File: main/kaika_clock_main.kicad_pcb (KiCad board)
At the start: 2 copper layers, 128 x 32 mm, 43 parts, among them J1 Conn_01x04, J6 Conn_01x04, SW1 TC-1102N-C-QL-B, SW2 SW-1101-B-W, SW3 TC-1102N-C-QL-B, U1 AMS1117-3.3, U2 STM32F103C8Tx, U3 DS3231MZ, U4 MICRO-USB_TH, U5 CR1220-2, U6 DS18B20, Y1 Crystal

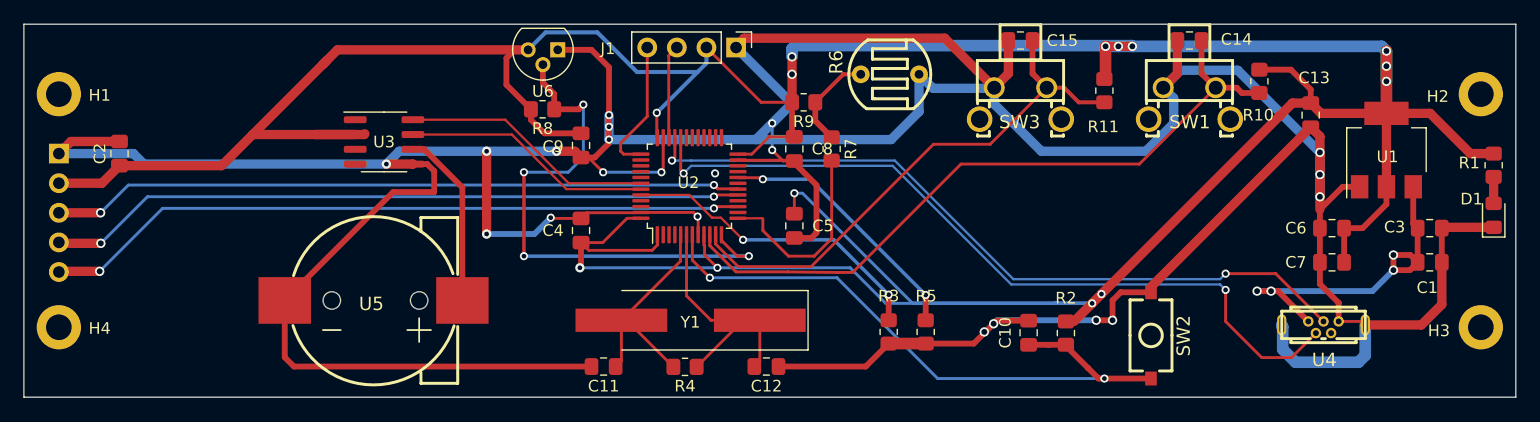
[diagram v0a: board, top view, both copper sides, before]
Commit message: modify the main and display
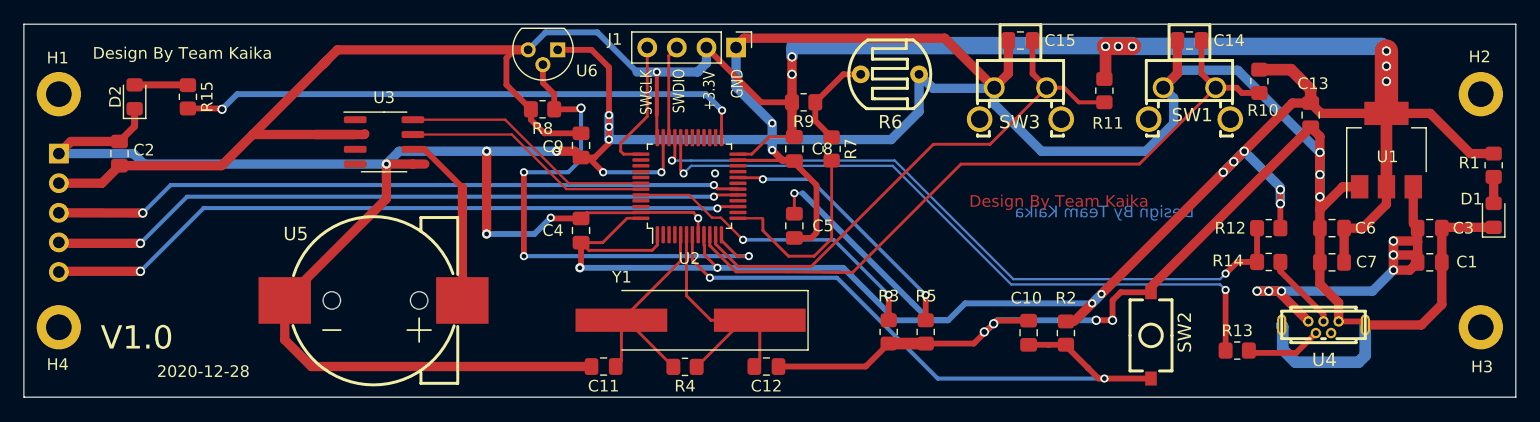
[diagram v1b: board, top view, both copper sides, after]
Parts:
- added D2: LED_Small, LED_SMD:LED_0805_2012Metric_Pad1.15x1.40mm_HandSolder, F.Cu at (109.5, 106.2)
- added R12: 1.5K, Resistor_SMD:R_0805_2012Metric_Pad1.20x1.40mm_HandSolder, F.Cu at (206.8, 117.5)
- added R13: 33, Resistor_SMD:R_0805_2012Metric_Pad1.20x1.40mm_HandSolder, F.Cu at (204.1, 128.0)
- added R14: 33, Resistor_SMD:R_0805_2012Metric_Pad1.20x1.40mm_HandSolder, F.Cu at (206.8, 120.4)
- added R15: 200, Resistor_SMD:R_0805_2012Metric_Pad1.20x1.40mm_HandSolder, F.Cu at (114.1, 106.2)
- J6: value Conn_01x04 -> Conn_01x05
- R6: value RES-GL7528 -> RES-GL7516
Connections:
- U2 pad 25: (no net) -> RUN_LED
- U2 pad 32: USB_D+ -> USB_D-
- U2 pad 33: USB_D- -> USB_D+
- U4 pad 2: USB_D+ -> Net-(R13-Pad1)
- U4 pad 3: USB_D- -> Net-(R14-Pad1)
- U4 pad 7: GND -> (no net)
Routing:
- net RUN_LED: track 0.00 -> 49.4 mm, vias 0 -> 2
- net GND: track 422.9 -> 414.6 mm
- net USB_D+: track 67.0 -> 60.0 mm
- net Net-(R14-Pad1): track 0.00 -> 6.63 mm
- net Net-(R13-Pad1): track 0.00 -> 6.54 mm
- net VCC: track 30.5 -> 36.2 mm, vias 4 -> 6
- net Net-(D2-Pad2): track 0.00 -> 4.58 mm
- net USB_D-: track 64.1 -> 59.5 mm
- net DS18B20: track 46.9 -> 46.2 mm
- net +3V3: track 351.6 -> 351.3 mm, vias 14 -> 19
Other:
- board text added: "+3.3V"
- board text added: "2020-12-28"
- board text added: "CS"
- board text added: "Design By Team Kaika"
- board text added: "GND"
- board text added: "MOSI"
- board text added: "SCK"
- board text added: "SWCLK"
- board text added: "SWDIO"
- board text added: "V1.0"
- board text added: "VCC"

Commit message: change usb footprint
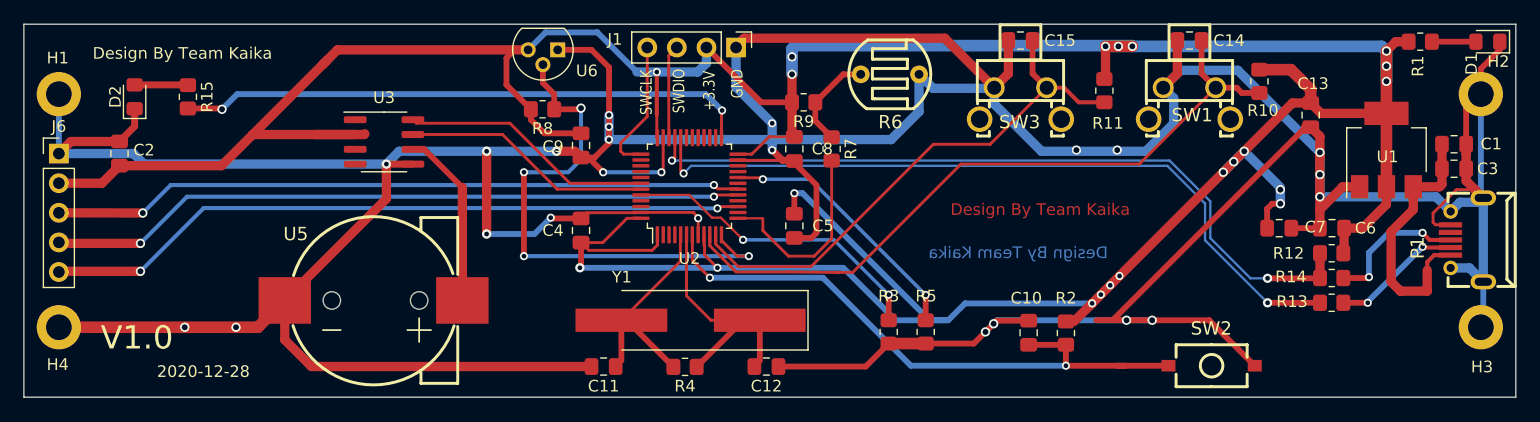
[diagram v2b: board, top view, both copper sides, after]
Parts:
- removed U4: MICRO-USB_TH, Kaka-footprints:MICRO-USB-TH_MICRO-USB-A14
- added P1: MICRO-USB_SMD, Kaka-footprints:MICRO-USB-SMD_MICRO-USB-18, F.Cu at (223.8, 118.5)
- J6: moved to F.Cu
- moved D1 14.9 mm to (225.6, 101.5), turned to 180 degrees
- moved R1 12.3 mm to (219.8, 101.5), turned to 180 degrees
- moved C1 10.3 mm to (222.7, 110.3)
- moved R13 9.08 mm to (212.2, 123.9)
- moved SW2 5.81 mm to (201.9, 129.3), turned to 0 degrees
- moved R12 5.81 mm to (212.2, 119.7)
- moved R14 5.57 mm to (212.2, 121.8)
- moved C3 5.51 mm to (222.7, 112.4)
- moved C7 5.39 mm to (207.7, 117.5), turned to 0 degrees
- turned J6 to 0 degrees
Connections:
- H1 pad 1: (no net) -> GND
- H2 pad 1: (no net) -> GND
- H3 pad 1: (no net) -> GND
- H4 pad 1: (no net) -> GND
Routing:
- net GND: track 414.6 -> 493.5 mm, vias 20 -> 24
- net VCC: track 36.2 -> 23.8 mm, vias 6 -> 0
- net +3V3: track 351.3 -> 345.2 mm, vias 19 -> 21
- net USB_D+: track 60.0 -> 65.9 mm
- net Net-(P1-Pad3): track 6.63 -> 12.3 mm, vias 0 -> 2
- net USB_D-: track 59.5 -> 64.7 mm
- net Net-(P1-Pad2): track 6.54 -> 11.3 mm, vias 0 -> 2
- net Net-(D1-Pad2): track 2.28 -> 3.77 mm
- net RESET: track 53.5 -> 53.0 mm
- net (no net): vias 1 -> 0

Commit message: update the main pcb
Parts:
- added C16: 100nf, Capacitor_SMD:C_0805_2012Metric_Pad1.18x1.45mm_HandSolder, F.Cu at (123.7, 112.0)
- added C17: 100nf, Capacitor_SMD:C_0805_2012Metric_Pad1.18x1.45mm_HandSolder, F.Cu at (143.5, 126.1)
- D2: value LED_Small -> D1
- R10, R11, R2: value R_Small -> 10K
- R8: value 0 -> 4.7K
- U6: footprint Package_TO_SOT_THT:TO-92 -> Package_TO_SOT_THT:TO-92_Inline
- moved R13 0.10 mm to (212.2, 123.8)
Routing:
- net GND: track 493.5 -> 502.2 mm, vias 24 -> 21
- net Net-(C17-Pad2): track 15.3 -> 21.7 mm
- net +3V3: track 345.2 -> 348.6 mm
- net Net-(P1-Pad3): track 12.3 -> 10.7 mm
- net DS18B20: track 46.2 -> 47.5 mm
- net KEY1: track 60.7 -> 61.3 mm
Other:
- board text added: "Kaikai&Kaka"
- board text added: "Lilili"

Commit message: add the gerber files
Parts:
- moved D2 5.12 mm to (107.8, 101.4), turned to 0 degrees
- moved R15 4.95 mm to (113.0, 101.4), turned to 0 degrees
- moved C2 1.45 mm to (109.6, 110.7)
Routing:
- net GND: track 502.2 -> 509.4 mm
- net RUN_LED: track 49.4 -> 52.5 mm
- net +3V3: track 348.6 -> 346.8 mm
- net Net-(D2-Pad2): track 4.58 -> 3.17 mm
- added copper zone on B.Cu, net GND
- added copper zone on F.Cu, net GND

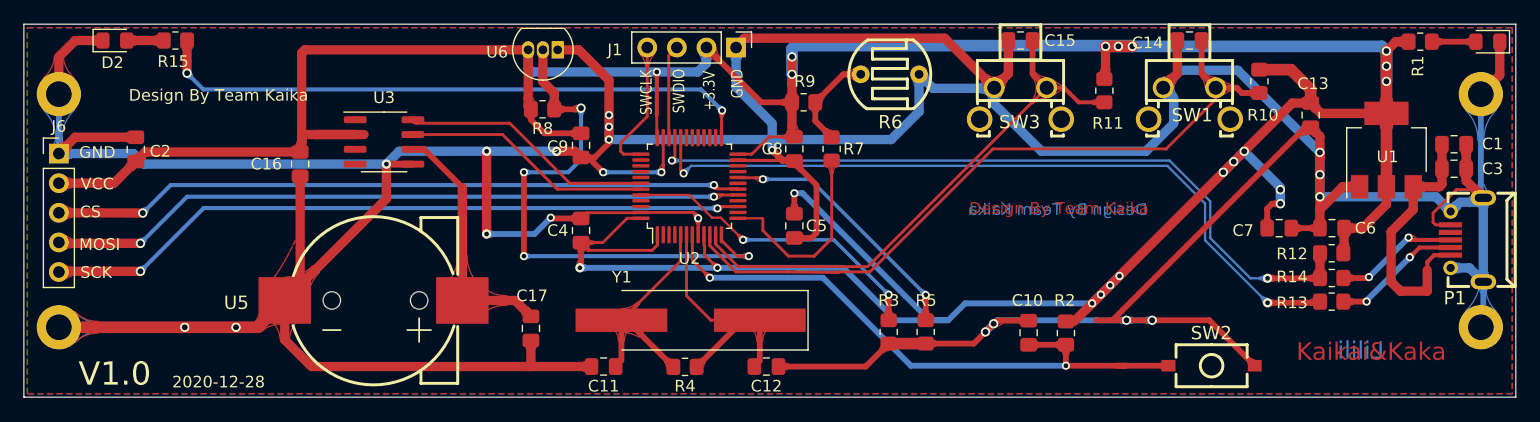
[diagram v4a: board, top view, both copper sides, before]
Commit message: modify display vcc to 5v and add the beep
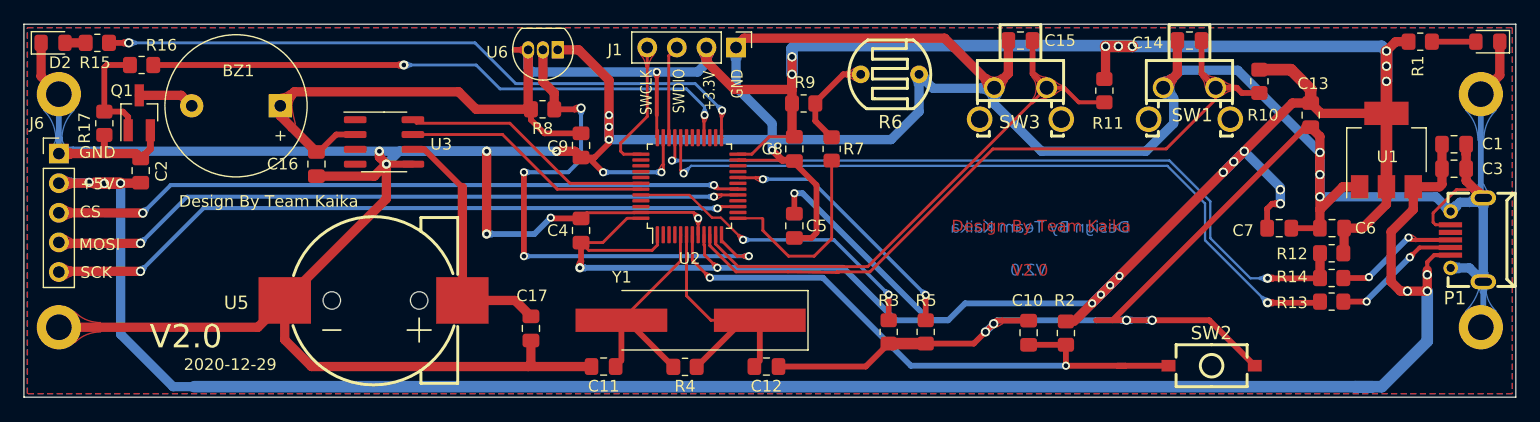
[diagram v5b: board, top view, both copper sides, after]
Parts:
- added BZ1: Buzzer, Buzzer_Beeper:Buzzer_12x9.5RM7.6, F.Cu at (122.0, 107.0)
- added Q1: Q_NPN_BEC, Package_TO_SOT_SMD:SOT-23_Handsoldering, F.Cu at (109.9, 107.6)
- added R16: 10K, Resistor_SMD:R_0805_2012Metric_Pad1.20x1.40mm_HandSolder, F.Cu at (110.1, 103.5)
- added R17: 1K, Resistor_SMD:R_0805_2012Metric_Pad1.20x1.40mm_HandSolder, F.Cu at (106.9, 108.5)
- moved R15 6.70 mm to (106.3, 101.6)
- moved D2 5.30 mm to (102.5, 101.6)
- moved C2 1.87 mm to (110.0, 112.6)
- moved C16 1.40 mm to (125.1, 112.0)
- moved R9 0.10 mm to (166.9, 106.8)
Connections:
- C2 pad 1: +3V3 -> VCC
- J6 pad 2: +3V3 -> VCC
- U2 pad 28: (no net) -> BEEP
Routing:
- net VCC: track 23.8 -> 170.5 mm, vias 0 -> 6
- net BEEP: track 0.00 -> 51.4 mm, vias 0 -> 2
- net +3V3: track 346.8 -> 319.4 mm
- net Net-(Q1-Pad1): track 0.00 -> 9.47 mm
- net GND: track 509.4 -> 502.7 mm, vias 21 -> 20
- net RUN_LED: track 52.5 -> 57.4 mm
- net Net-(BZ1-Pad2): track 0.00 -> 4.87 mm
- net Net-(D2-Pad2): track 3.17 -> 1.77 mm
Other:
- board text added: "+5V"
- board text added: "2020-12-29"
- board text added: "V2.0"
- board text removed: "2020-12-28"
- board text removed: "Kaikai&Kaka"
- board text removed: "Lilili"
- board text removed: "V1.0"
- board text removed: "VCC"

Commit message: modify the main
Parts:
- added C18: 10uf, Capacitor_SMD:C_1210_3225Metric_Pad1.33x2.70mm_HandSolder, F.Cu at (217.3, 127.2)
- SW2: footprint Kaka-footprints:KEY-SMD_2P-L6.0-W3.6-P7.4-LS8.0-L -> Kaka-footprints:SW-SMD_L6.2-W3.6-LS8.0
- moved SW2 1.64 mm to (200.6, 128.3)
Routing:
- net VCC: track 170.5 -> 174.8 mm, vias 6 -> 7
- net GND: track 502.7 -> 504.6 mm, vias 20 -> 21
- net RESET: track 53.0 -> 51.2 mm
- net +3V3: track 319.4 -> 318.3 mm
- added copper zone on B.Cu, net VCC
- added copper zone on F.Cu, net VCC

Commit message: modify the bat footprints
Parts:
- removed U5: CR1220-2, Kaka-footprints:BAT-SMD_CR1220-2
- added BT1: Battery_Cell, Kaka-footprints:BAT-SMD_CR2032-3V, F.Cu at (128.4, 121.8)
- R1: value 330 -> 200
- R7: value 0 -> 1K
- R9: value 0 -> 22K
- moved C16 4.79 mm to (127.0, 107.6)
- moved U3 3.36 mm to (132.6, 107.2)
- moved C17 2.86 mm to (141.9, 128.5)
- moved BZ1 0.32 mm to (122.3, 106.9)
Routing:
- net Net-(BT1-Pad1): track 21.7 -> 64.2 mm, vias 0 -> 4
- net +3V3: track 318.3 -> 313.0 mm
- net VCC: track 174.8 -> 180.0 mm
- net DS18B20: track 47.5 -> 45.4 mm
- net GND: track 504.6 -> 505.6 mm, vias 21 -> 23
- removed copper zone on B.Cu, net VCC
- removed copper zone on F.Cu, net VCC

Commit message: modify main pcb
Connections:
- P1 pad 4: (no net) -> Net-(P1-Pad4)
- SW1 pad 3: (no net) -> Net-(SW1-Pad3)
- SW1 pad 4: (no net) -> Net-(SW1-Pad4)
- SW3 pad 3: (no net) -> Net-(SW3-Pad3)
- SW3 pad 4: (no net) -> Net-(SW3-Pad4)
- U2 pad 14: (no net) -> Net-(U2-Pad14)
- U2 pad 16: (no net) -> Net-(U2-Pad16)
- U2 pad 19: (no net) -> Net-(U2-Pad19)
- U2 pad 2: (no net) -> Net-(U2-Pad2)
- U2 pad 21: (no net) -> Net-(U2-Pad21)
- U2 pad 22: (no net) -> Net-(U2-Pad22)
- U2 pad 25: RUN_LED -> Net-(U2-Pad25)
- U2 pad 26: (no net) -> RUN_LED
- U2 pad 27: (no net) -> Net-(U2-Pad27)
- U2 pad 29: (no net) -> Net-(U2-Pad29)
- U2 pad 3: (no net) -> Net-(U2-Pad3)
- U2 pad 30: (no net) -> Net-(U2-Pad30)
- U2 pad 31: (no net) -> Net-(U2-Pad31)
- U2 pad 38: (no net) -> Net-(U2-Pad38)
- U2 pad 39: (no net) -> Net-(U2-Pad39)
- U2 pad 4: (no net) -> Net-(U2-Pad4)
- U2 pad 40: (no net) -> Net-(U2-Pad40)
- U2 pad 41: (no net) -> Net-(U2-Pad41)
- U2 pad 45: (no net) -> Net-(U2-Pad45)
- U2 pad 46: (no net) -> Net-(U2-Pad46)
- U3 pad 1: (no net) -> Net-(U3-Pad1)
- U3 pad 3: (no net) -> Net-(U3-Pad3)
- U3 pad 4: (no net) -> Net-(U3-Pad4)
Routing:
- net GND: track 505.6 -> 543.5 mm, vias 23 -> 39
